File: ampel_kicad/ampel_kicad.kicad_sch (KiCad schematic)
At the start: 16 parts, among them J1 Power, J2 Digital/PWM, J3 Analog, J4 Digital/PWM, J5 Conn_Extern, J6 Conn_Main, SW1 SW_Push

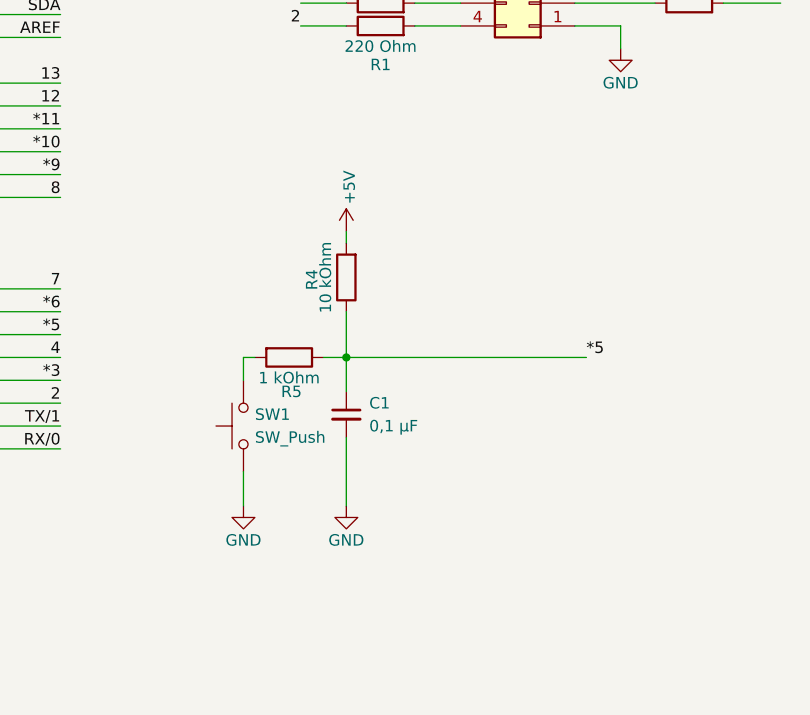
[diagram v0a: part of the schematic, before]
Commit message: update: no debounce
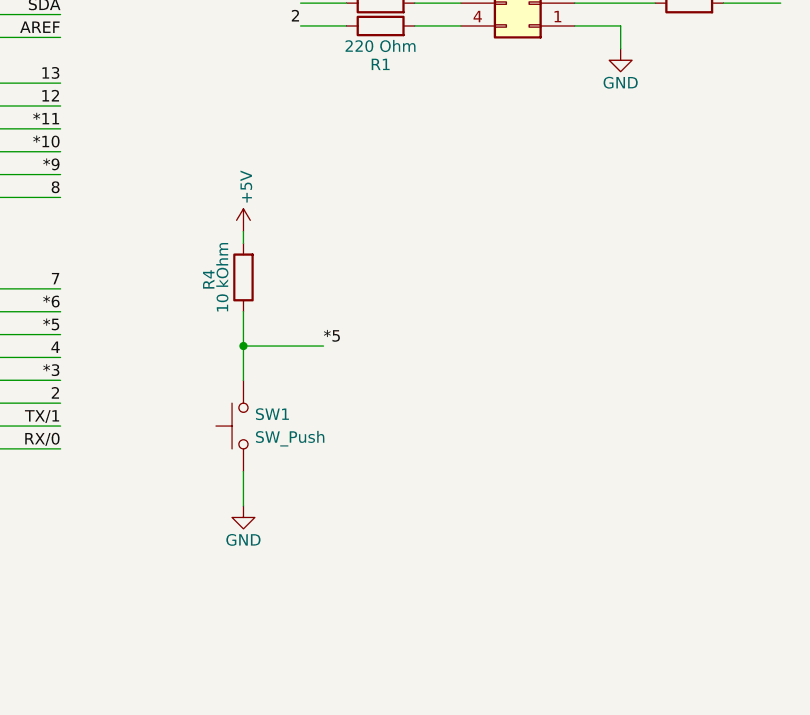
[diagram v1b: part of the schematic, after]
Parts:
- removed C1: 0,1 µF, Capacitor_THT:C_Axial_L5.1mm_D3.1mm_P7.50mm_Horizontal, symbol Device:C_Small
- removed R5: 1 kOhm, Resistor_THT:R_Axial_DIN0207_L6.3mm_D2.5mm_P7.62mm_Horizontal, symbol Device:R
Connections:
- net *5: now also SW1.2
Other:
- moved on the sheet: R4
